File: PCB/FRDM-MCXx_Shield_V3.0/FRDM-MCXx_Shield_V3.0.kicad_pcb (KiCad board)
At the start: 4 copper layers, 54.3 x 54.7 mm, 89 parts, among them J1 Conn_02x08_Odd_Even, J2 Conn_02x06_Odd_Even, J3 Conn_02x10_Odd_Even, J4 Conn_02x08_Odd_Even, J5 Conn_01x04_Socket, J6 Conn_01x04_Pin, J7 Conn_01x04_Pin, J8 Conn_01x04_Pin, M1 Motor_Servo, SW1 EC12D1524406, U1 74HC595, U2 M95010-RMN6TP, U3 LM35-D

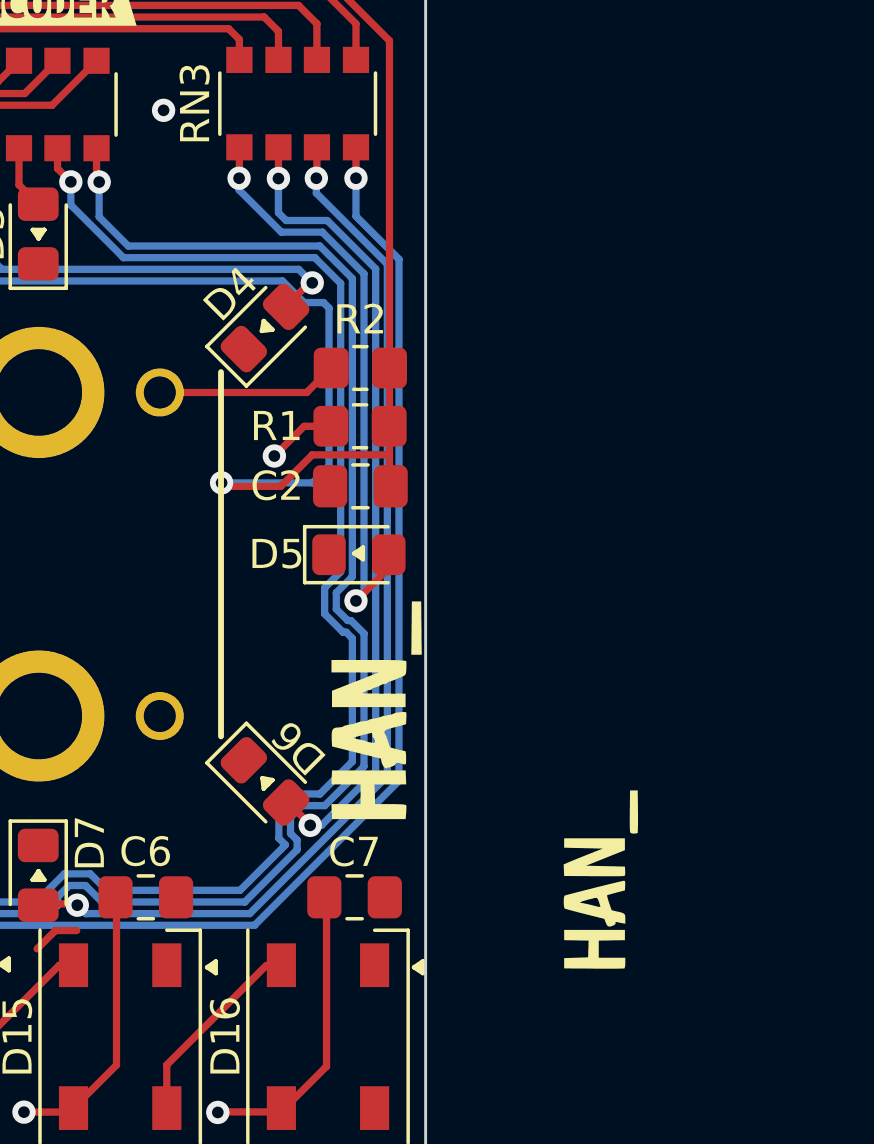
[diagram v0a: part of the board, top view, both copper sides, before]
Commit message: Updated labeling. removed code
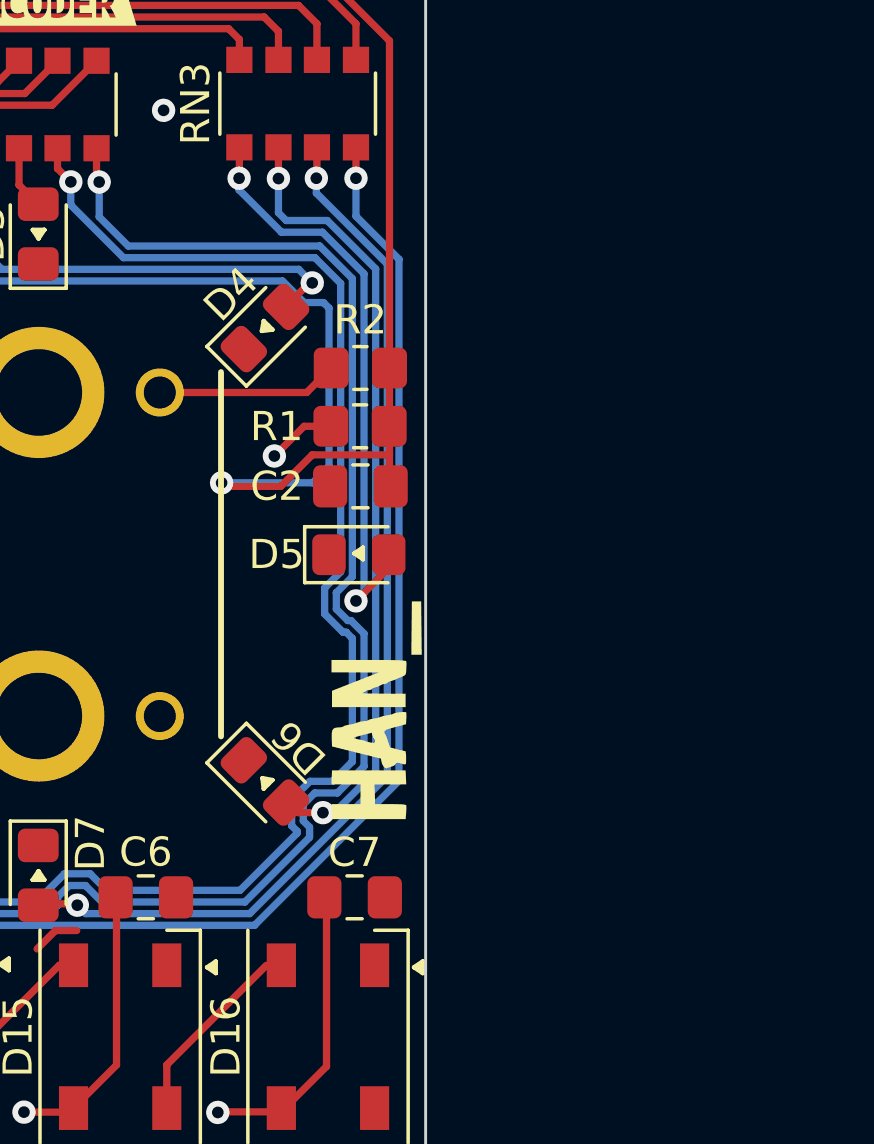
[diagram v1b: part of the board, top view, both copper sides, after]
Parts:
- removed the G*** at (187.8, 102.1)
- moved G*** 16.8 mm to (178.1, 103.4)

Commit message: Added R7
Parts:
- added R7: 470, Resistor_SMD:R_0805_2012Metric_Pad1.20x1.40mm_HandSolder, F.Cu at (160.4, 106.0)
- moved TP2 0.78 mm to (156.5, 101.2)
- moved TP6 0.40 mm to (158.2, 109.5)
- moved TP5 0.38 mm to (158.2, 105.0)
- renumbered R7 to R8, R8 to R9
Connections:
- D14 pad 2: /LED_NEOPIXEL -> Net-(D14-DIN)
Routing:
- net GND: track 3.92 -> 17.2 mm
- net +3.3V: track 270.1 -> 267.3 mm
- net Net-(D14-DIN): track 0.00 -> 2.17 mm
